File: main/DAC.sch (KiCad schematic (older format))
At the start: 14 parts, among them IC1 PCM1741E, J12 Breakout I2S

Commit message: Final cleanup before sending in for rebiew
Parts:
- renumbered C40 to C25, C42 to C26, IC1 to IC3, J12 to J7, R36 to R22, R14 to R23, R37 to R24, R38 to R25, R15 to R26, R39 to R27, R40 to R28, R16 to R29, R41 to R30, R17 to R31
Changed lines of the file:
@@
 AR Path="/6149F240" Ref="R?"  Part="1"
 AR Path="/61417224/6149F240" Ref="R?"  Part="1"
-AR Path="/61496F7B/6149F240" Ref="R15"  Part="1"
-F 0 "R15" V 3350 3300 50  0000 C CNN
+AR Path="/61496F7B/6149F240" Ref="R26"  Part="1"
+F 0 "R26" V 3350 3300 50  0000 C CNN
 F 1 "22-100" V 3250 3300 50  0000 C CNN
 F 2 "" V 3280 3300 50  0001 C CNN
@@
 AR Path="/6149F246" Ref="R?"  Part="1"
 AR Path="/61417224/6149F246" Ref="R?"  Part="1"
-AR Path="/61496F7B/6149F246" Ref="R14"  Part="1"
-F 0 "R14" V 3050 3300 50  0000 C CNN
+AR Path="/61496F7B/6149F246" Ref="R23"  Part="1"
+F 0 "R23" V 3050 3300 50  0000 C CNN
 F 1 "22-100" V 2950 3300 50  0000 C CNN
 F 2 "" V 2980 3300 50  0001 C CNN
@@
 AR Path="/6149F24C" Ref="R?"  Part="1"
 AR Path="/61417224/6149F24C" Ref="R?"  Part="1"
-AR Path="/61496F7B/6149F24C" Ref="R16"  Part="1"
-F 0 "R16" V 3650 3300 50  0000 C CNN
+AR Path="/61496F7B/6149F24C" Ref="R29"  Part="1"
+F 0 "R29" V 3650 3300 50  0000 C CNN
 F 1 "22-100" V 3550 3300 50  0000 C CNN
 F 2 "" V 3580 3300 50  0001 C CNN
@@
 AR Path="/614A0D57" Ref="R?"  Part="1"
 AR Path="/61417224/614A0D57" Ref="R?"  Part="1"
-AR Path="/61496F7B/614A0D57" Ref="R17"  Part="1"
-F 0 "R17" V 7800 2950 50  0000 C CNN
+AR Path="/61496F7B/614A0D57" Ref="R31"  Part="1"
+F 0 "R31" V 7800 2950 50  0000 C CNN
 F 1 "22-100" V 7700 2950 50  0000 C CNN
 F 2 "" V 7730 2950 50  0001 C CNN
@@
 	7950 2950 8100 2950
 $Comp
-L Device:CP1 C42
+L Device:CP1 C26
 U 1 1 614A3178
 P 7250 4400
-F 0 "C42" H 7365 4446 50  0000 L CNN
+F 0 "C26" H 7365 4446 50  0000 L CNN
 F 1 "10uF" H 7365 4355 50  0000 L CNN
 F 2 "" H 7250 4400 50  0001 C CNN
@@
 	6550 4250 7250 4250
 $Comp
-L power:GNDA #PWR0149
+L power:GNDA #PWR025
 U 1 1 614A4529
 P 7250 4600
-F 0 "#PWR0149" H 7250 4350 50  0001 C CNN
+F 0 "#PWR025" H 7250 4350 50  0001 C CNN
 F 1 "GNDA" H 7255 4427 50  0000 C CNN
 F 2 "" H 7250 4600 50  0001 C CNN
@@
 	3650 2800 3650 3150
 $Comp
-L Device:R R36
+L Device:R R22
 U 1 1 614FAF80
 P 3050 2500
-F 0 "R36" H 2900 2350 50  0000 L CNN
+F 0 "R22" H 2900 2350 50  0000 L CNN
 F 1 "0" H 3050 2350 50  0000 L CNN
 F 2 "" V 2980 2500 50  0001 C CNN
@@
 	3050 2650 3050 2800
 $Comp
-L Device:R R37
+L Device:R R24
 U 1 1 614FB4C3
 P 3150 2500
-F 0 "R37" H 3150 2650 50  0000 L CNN
+F 0 "R24" H 3150 2650 50  0000 L CNN
 F 1 "0" H 3150 2350 50  0000 L CNN
 F 2 "" V 3080 2500 50  0001 C CNN
@@
 	3150 2350 3150 1800
 $Comp
-L Device:R R38
+L Device:R R25
 U 1 1 614FB6C2
 P 3350 2500
-F 0 "R38" H 3200 2350 50  0000 L CNN
+F 0 "R25" H 3200 2350 50  0000 L CNN
 F 1 "0" H 3350 2350 50  0000 L CNN
 F 2 "" V 3280 2500 50  0001 C CNN
@@
 	3350 2650 3350 2800
 $Comp
-L Device:R R39
+L Device:R R27
 U 1 1 614FB93A
 P 3450 2500
-F 0 "R39" H 3450 2650 50  0000 L CNN
+F 0 "R27" H 3450 2650 50  0000 L CNN
 F 1 "0" H 3450 2350 50  0000 L CNN
 F 2 "" V 3380 2500 50  0001 C CNN
@@
 $EndComp
 $Comp
-L Device:R R40
+L Device:R R28
 U 1 1 614FBC49
 P 3650 2500
-F 0 "R40" H 3500 2350 50  0000 L CNN
+F 0 "R28" H 3500 2350 50  0000 L CNN
 F 1 "0" H 3650 2350 50  0000 L CNN
 F 2 "" V 3580 2500 50  0001 C CNN
@@
 	3650 2650 3650 2800
 $Comp
-L Device:R R41
+L Device:R R30
 U 1 1 614FBF3E
 P 3750 2500
-F 0 "R41" H 3750 2650 50  0000 L CNN
+F 0 "R30" H 3750 2650 50  0000 L CNN
 F 1 "0" H 3750 2350 50  0000 L CNN
 F 2 "" V 3680 2500 50  0001 C CNN
@@
 If we fry the onboard FPGA and \nhave to use a separate one, we \ncan wire the 0 ohm resistors to \nthe breakout I2S pins.
 $Comp
-L Connector:Conn_01x03_Male J12
+L Connector:Conn_01x03_Male J7
 U 1 1 614FD08E
 P 3450 1450
-F 0 "J12" V 3512 1594 50  0000 L CNN
+F 0 "J7" V 3512 1594 50  0000 L CNN
 F 1 "Breakout I2S" V 3603 1594 50  0000 L CNN
 F 2 "" H 3450 1450 50  0001 C CNN
@@
 	4700 4450 4600 4450
 $Comp
-L power:+3.3VA #PWR0168
+L power:+3.3VA #PWR024
 U 1 1 6150F536
 P 4600 4450
-F 0 "#PWR0168" H 4600 4300 50  0001 C CNN
+F 0 "#PWR024" H 4600 4300 50  0001 C CNN
 F 1 "+3.3VA" V 4615 4577 50  0000 L CNN
 F 2 "" H 4600 4450 50  0001 C CNN
@@
 $EndComp
 $Comp
-L power:+3.3V #PWR0169
+L power:+3.3V #PWR023
 U 1 1 6151042C
 P 3700 4250
-F 0 "#PWR0169" H 3700 4100 50  0001 C CNN
+F 0 "#PWR023" H 3700 4100 50  0001 C CNN
 F 1 "+3.3V" V 3715 4378 50  0000 L CNN
 F 2 "" H 3700 4250 50  0001 C CNN
@@
 	5250 2300 2900 2300
 $Comp
-L Device:CP1 C40
+L Device:CP1 C25
 U 1 1 615EACC2
 P 4000 4100
-F 0 "C40" H 4115 4146 50  0000 L CNN
+F 0 "C25" H 4115 4146 50  0000 L CNN
 F 1 "10uF" H 4115 4055 50  0000 L CNN
 F 2 "" H 4000 4100 50  0001 C CNN
@@
 	4000 4250 3700 4250
 $Comp
-L power:GND #PWR0170
+L power:GND #PWR022
 U 1 1 6151148F
 P 3650 3950
-F 0 "#PWR0170" H 3650 3700 50  0001 C CNN
+F 0 "#PWR022" H 3650 3700 50  0001 C CNN
 F 1 "GND" V 3655 3822 50  0000 R CNN
 F 2 "" H 3650 3950 50  0001 C CNN
@@
 	4000 3950 5050 3950
 $Comp
-L PCM1741E:PCM1741E IC1
+L PCM1741E:PCM1741E IC3
 U 1 1 614975F8
 P 5050 3650
-F 0 "IC1" H 5800 3915 50  0000 C CNN
+F 0 "IC3" H 5800 3915 50  0000 C CNN
 F 1 "PCM1741E" H 5800 3824 50  0000 C CNN
 F 2 "DAC:SOP63P600X175-16N" H 6400 3750 50  0001 L CNN

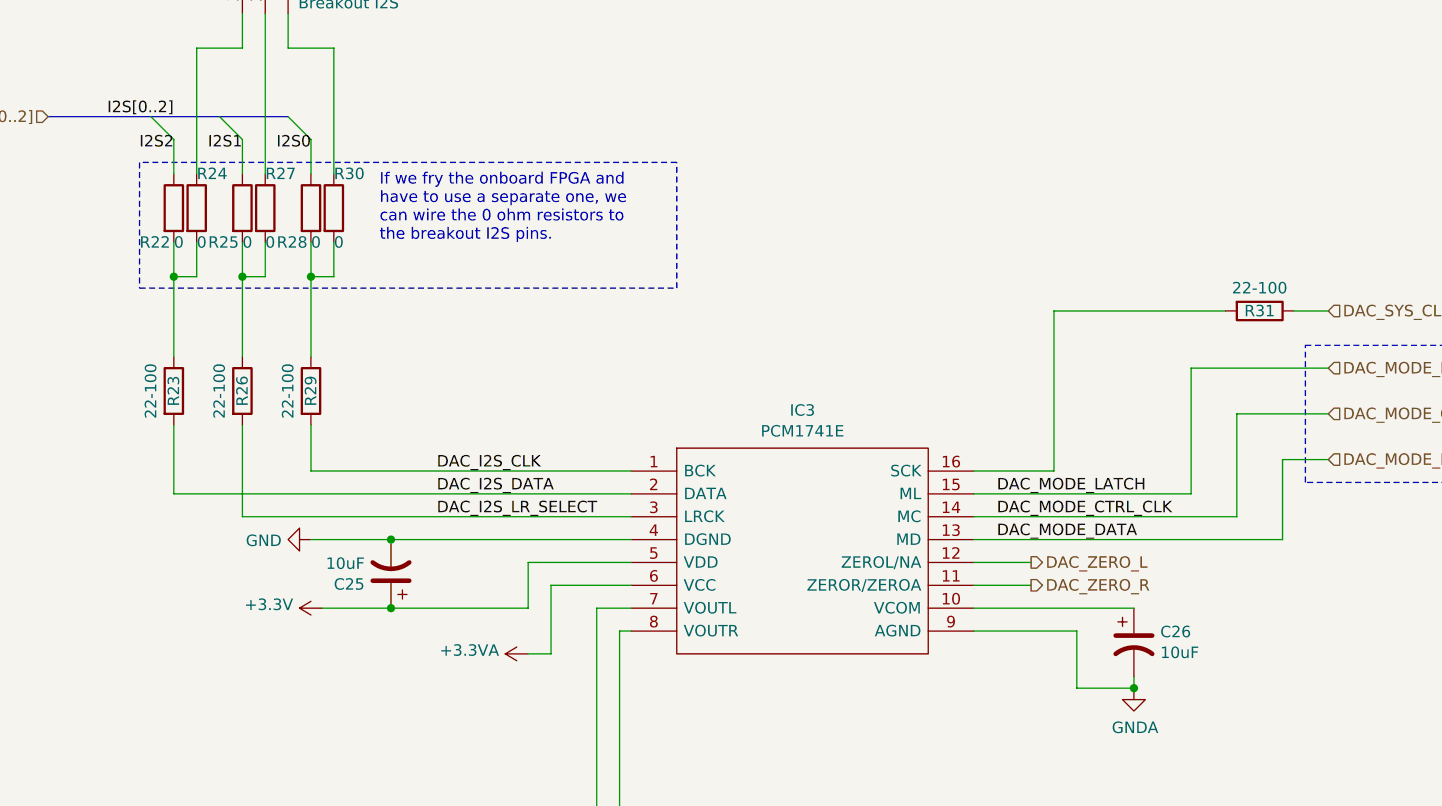
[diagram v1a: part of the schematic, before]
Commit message: Fix up after review
Done:
- Add bulk decoupling capacitor to switch regulator cirucit
- Disconnect DONE from PROGRAM_B in FPGA (mistake)
- The decoupling capacitors used for the FPGA were for the 15T, not the
  100T. It was also setup for two I/O banks, we only use one. Disconnect
  I/O bank 15.
- Switch external clock on the MCU to an oscillator, allowing for 72MHz
- Switch pinout of the backup SPI on the MCU so that half the pins are
  ground

Mizzing:
- Add low-pass filters to the output of the DAC as per the datasheet.
  May remove the need for the amplifier circuit.
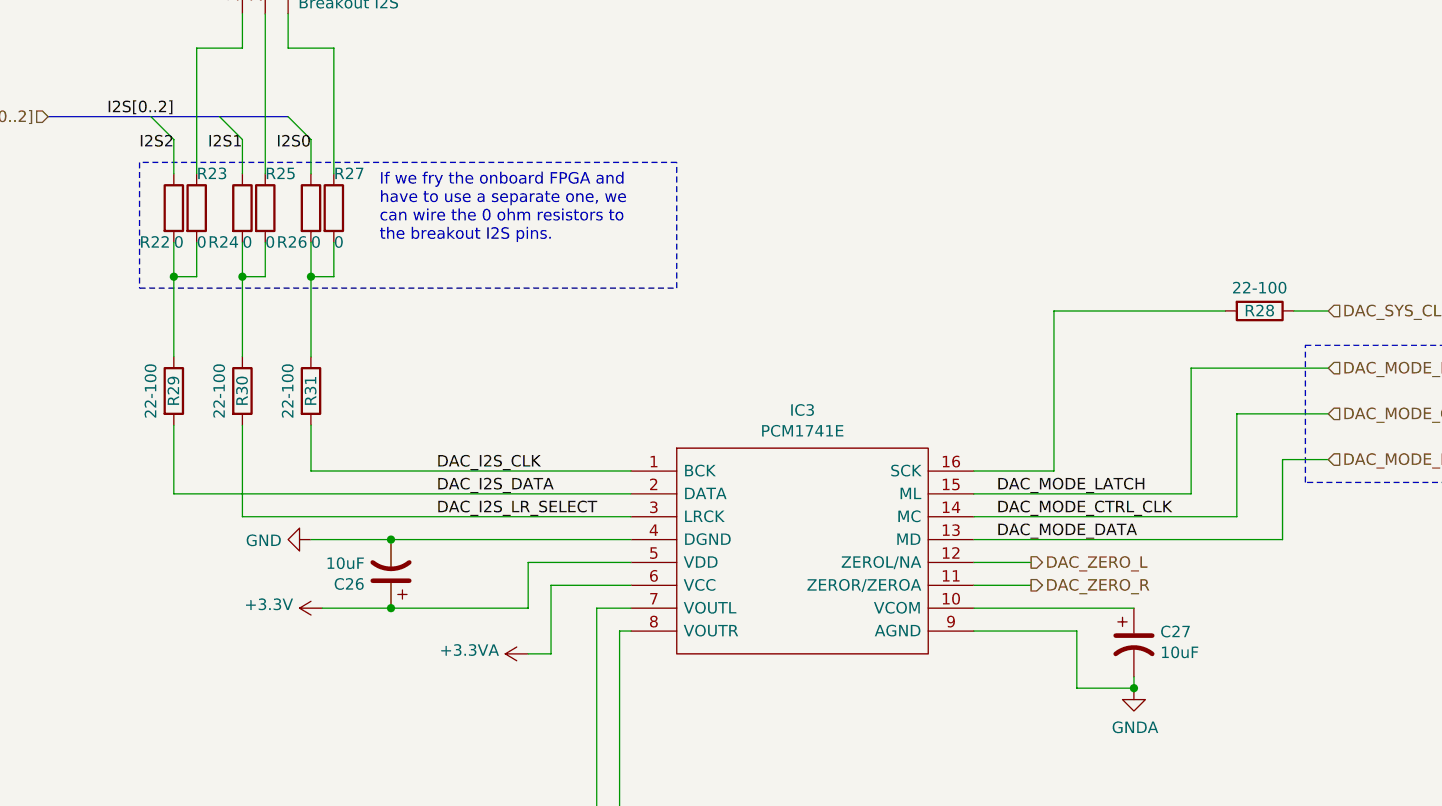
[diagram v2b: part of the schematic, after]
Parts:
- R22: footprint (none) -> Jumper:SolderJumper-2_P1.3mm_Bridged2Bar_RoundedPad1.0x1.5mm
- R23: renamed from R24; footprint (none) -> Jumper:SolderJumper-2_P1.3mm_Open_RoundedPad1.0x1.5mm
- R24: renamed from R25; footprint (none) -> Jumper:SolderJumper-2_P1.3mm_Bridged2Bar_RoundedPad1.0x1.5mm
- R25: renamed from R27; footprint (none) -> Jumper:SolderJumper-2_P1.3mm_Open_RoundedPad1.0x1.5mm
- R26: renamed from R28; footprint (none) -> Jumper:SolderJumper-2_P1.3mm_Bridged2Bar_RoundedPad1.0x1.5mm
- R27: renamed from R30; footprint (none) -> Jumper:SolderJumper-2_P1.3mm_Open_RoundedPad1.0x1.5mm
- R28: renamed from R31; footprint (none) -> Resistor_SMD:R_0805_2012Metric_Pad1.20x1.40mm_HandSolder
- R29: renamed from R23; footprint (none) -> Resistor_SMD:R_0805_2012Metric_Pad1.20x1.40mm_HandSolder
- R30: renamed from R26; footprint (none) -> Resistor_SMD:R_0805_2012Metric_Pad1.20x1.40mm_HandSolder
- R31: renamed from R29; footprint (none) -> Resistor_SMD:R_0805_2012Metric_Pad1.20x1.40mm_HandSolder
- renumbered C25 to C26, C26 to C27
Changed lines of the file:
@@
 AR Path="/6149F240" Ref="R?"  Part="1"
 AR Path="/61417224/6149F240" Ref="R?"  Part="1"
-AR Path="/61496F7B/6149F240" Ref="R26"  Part="1"
-F 0 "R26" V 3350 3300 50  0000 C CNN
+AR Path="/61496F7B/6149F240" Ref="R30"  Part="1"
+F 0 "R30" V 3350 3300 50  0000 C CNN
 F 1 "22-100" V 3250 3300 50  0000 C CNN
-F 2 "" V 3280 3300 50  0001 C CNN
+F 2 "Resistor_SMD:R_0805_2012Metric_Pad1.20x1.40mm_HandSolder" V 3280 3300 50  0001 C CNN
 F 3 "~" H 3350 3300 50  0001 C CNN
 	1    3350 3300
@@
 AR Path="/6149F246" Ref="R?"  Part="1"
 AR Path="/61417224/6149F246" Ref="R?"  Part="1"
-AR Path="/61496F7B/6149F246" Ref="R23"  Part="1"
-F 0 "R23" V 3050 3300 50  0000 C CNN
+AR Path="/61496F7B/6149F246" Ref="R29"  Part="1"
+F 0 "R29" V 3050 3300 50  0000 C CNN
 F 1 "22-100" V 2950 3300 50  0000 C CNN
-F 2 "" V 2980 3300 50  0001 C CNN
+F 2 "Resistor_SMD:R_0805_2012Metric_Pad1.20x1.40mm_HandSolder" V 2980 3300 50  0001 C CNN
 F 3 "~" H 3050 3300 50  0001 C CNN
 	1    3050 3300
@@
 AR Path="/6149F24C" Ref="R?"  Part="1"
 AR Path="/61417224/6149F24C" Ref="R?"  Part="1"
-AR Path="/61496F7B/6149F24C" Ref="R29"  Part="1"
-F 0 "R29" V 3650 3300 50  0000 C CNN
+AR Path="/61496F7B/6149F24C" Ref="R31"  Part="1"
+F 0 "R31" V 3650 3300 50  0000 C CNN
 F 1 "22-100" V 3550 3300 50  0000 C CNN
-F 2 "" V 3580 3300 50  0001 C CNN
+F 2 "Resistor_SMD:R_0805_2012Metric_Pad1.20x1.40mm_HandSolder" V 3580 3300 50  0001 C CNN
 F 3 "~" H 3650 3300 50  0001 C CNN
 	1    3650 3300
@@
 AR Path="/614A0D57" Ref="R?"  Part="1"
 AR Path="/61417224/614A0D57" Ref="R?"  Part="1"
-AR Path="/61496F7B/614A0D57" Ref="R31"  Part="1"
-F 0 "R31" V 7800 2950 50  0000 C CNN
+AR Path="/61496F7B/614A0D57" Ref="R28"  Part="1"
+F 0 "R28" V 7800 2950 50  0000 C CNN
 F 1 "22-100" V 7700 2950 50  0000 C CNN
-F 2 "" V 7730 2950 50  0001 C CNN
+F 2 "Resistor_SMD:R_0805_2012Metric_Pad1.20x1.40mm_HandSolder" V 7730 2950 50  0001 C CNN
 F 3 "~" H 7800 2950 50  0001 C CNN
 	1    7800 2950
@@
 	7950 2950 8100 2950
 $Comp
-L Device:CP1 C26
+L Device:CP1 C27
 U 1 1 614A3178
 P 7250 4400
-F 0 "C26" H 7365 4446 50  0000 L CNN
+F 0 "C27" H 7365 4446 50  0000 L CNN
 F 1 "10uF" H 7365 4355 50  0000 L CNN
 F 2 "" H 7250 4400 50  0001 C CNN
@@
 F 0 "R22" H 2900 2350 50  0000 L CNN
 F 1 "0" H 3050 2350 50  0000 L CNN
-F 2 "" V 2980 2500 50  0001 C CNN
+F 2 "Jumper:SolderJumper-2_P1.3mm_Bridged2Bar_RoundedPad1.0x1.5mm" V 2980 2500 50  0001 C CNN
 F 3 "~" H 3050 2500 50  0001 C CNN
 	1    3050 2500
@@
 	3050 2650 3050 2800
 $Comp
-L Device:R R24
+L Device:R R23
 U 1 1 614FB4C3
 P 3150 2500
-F 0 "R24" H 3150 2650 50  0000 L CNN
+F 0 "R23" H 3150 2650 50  0000 L CNN
 F 1 "0" H 3150 2350 50  0000 L CNN
-F 2 "" V 3080 2500 50  0001 C CNN
+F 2 "Jumper:SolderJumper-2_P1.3mm_Open_RoundedPad1.0x1.5mm" V 3080 2500 50  0001 C CNN
 F 3 "~" H 3150 2500 50  0001 C CNN
 	1    3150 2500
@@
 	3150 2350 3150 1800
 $Comp
-L Device:R R25
+L Device:R R24
 U 1 1 614FB6C2
 P 3350 2500
-F 0 "R25" H 3200 2350 50  0000 L CNN
+F 0 "R24" H 3200 2350 50  0000 L CNN
 F 1 "0" H 3350 2350 50  0000 L CNN
-F 2 "" V 3280 2500 50  0001 C CNN
+F 2 "Jumper:SolderJumper-2_P1.3mm_Bridged2Bar_RoundedPad1.0x1.5mm" V 3280 2500 50  0001 C CNN
 F 3 "~" H 3350 2500 50  0001 C CNN
 	1    3350 2500
@@
 	3350 2650 3350 2800
 $Comp
-L Device:R R27
+L Device:R R25
 U 1 1 614FB93A
 P 3450 2500
-F 0 "R27" H 3450 2650 50  0000 L CNN
+F 0 "R25" H 3450 2650 50  0000 L CNN
 F 1 "0" H 3450 2350 50  0000 L CNN
-F 2 "" V 3380 2500 50  0001 C CNN
+F 2 "Jumper:SolderJumper-2_P1.3mm_Open_RoundedPad1.0x1.5mm" V 3380 2500 50  0001 C CNN
 F 3 "~" H 3450 2500 50  0001 C CNN
 	1    3450 2500
@@
 $EndComp
 $Comp
-L Device:R R28
+L Device:R R26
 U 1 1 614FBC49
 P 3650 2500
-F 0 "R28" H 3500 2350 50  0000 L CNN
+F 0 "R26" H 3500 2350 50  0000 L CNN
 F 1 "0" H 3650 2350 50  0000 L CNN
-F 2 "" V 3580 2500 50  0001 C CNN
+F 2 "Jumper:SolderJumper-2_P1.3mm_Bridged2Bar_RoundedPad1.0x1.5mm" V 3580 2500 50  0001 C CNN
 F 3 "~" H 3650 2500 50  0001 C CNN
 	1    3650 2500
@@
 	3650 2650 3650 2800
 $Comp
-L Device:R R30
+L Device:R R27
 U 1 1 614FBF3E
 P 3750 2500
-F 0 "R30" H 3750 2650 50  0000 L CNN
+F 0 "R27" H 3750 2650 50  0000 L CNN
 F 1 "0" H 3750 2350 50  0000 L CNN
-F 2 "" V 3680 2500 50  0001 C CNN
+F 2 "Jumper:SolderJumper-2_P1.3mm_Open_RoundedPad1.0x1.5mm" V 3680 2500 50  0001 C CNN
 F 3 "~" H 3750 2500 50  0001 C CNN
 	1    3750 2500
@@
 	5250 2300 2900 2300
 $Comp
-L Device:CP1 C25
+L Device:CP1 C26
 U 1 1 615EACC2
 P 4000 4100
-F 0 "C25" H 4115 4146 50  0000 L CNN
+F 0 "C26" H 4115 4146 50  0000 L CNN
 F 1 "10uF" H 4115 4055 50  0000 L CNN
 F 2 "" H 4000 4100 50  0001 C CNN

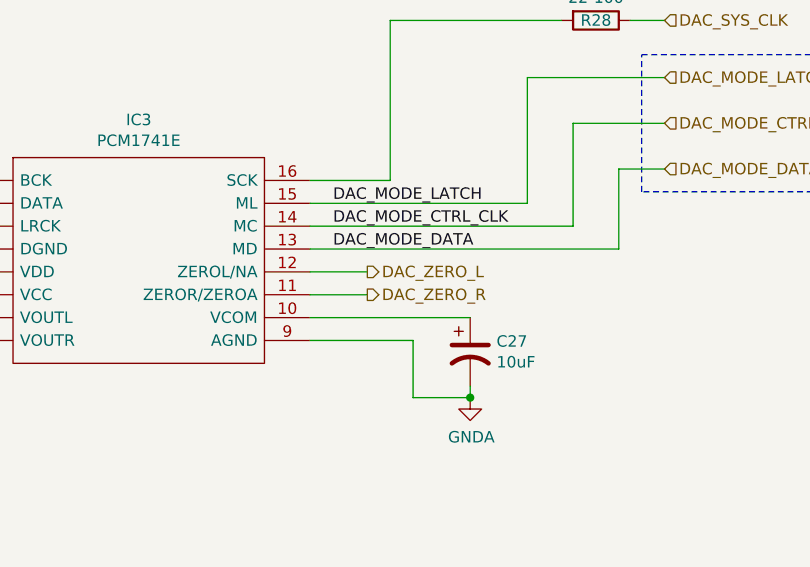
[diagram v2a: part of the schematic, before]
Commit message: Fix up after review 2
Don't route DAC_ZERO_{L,R} through FPGA into SHUTDOWN on the amp, it is
not really necessary and just adds routing complexity.
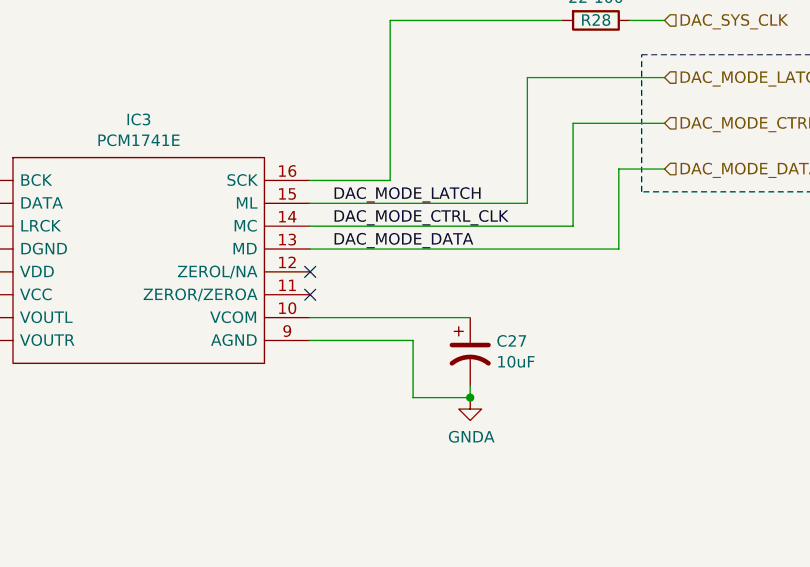
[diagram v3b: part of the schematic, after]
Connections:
- net DAC_ZERO_L: no longer names the net of IC3.12 (ZEROL/NA)
- net DAC_ZERO_R: no longer names the net of IC3.11 (ZEROR/ZEROA)
- no-connect marks 0 -> 2
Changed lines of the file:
@@
 	1    0    0    -1
 $EndComp
-Text HLabel 6800 4050 2    50   Output ~ 0
-DAC_ZERO_L
-Wire Wire Line
-	6800 4050 6550 4050
-Wire Wire Line
-	6550 4150 6800 4150
-Text HLabel 6800 4150 2    50   Output ~ 0
-DAC_ZERO_R
 Wire Wire Line
 	3050 2200 3050 2350
+NoConn ~ 6550 4050
+NoConn ~ 6550 4150
 Wire Bus Line
 	2500 2100 3550 2100
